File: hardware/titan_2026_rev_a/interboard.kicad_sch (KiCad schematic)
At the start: 7 parts, among them J7 B7B-XH, J8 B7B-XH, U4 ISO1642DWR

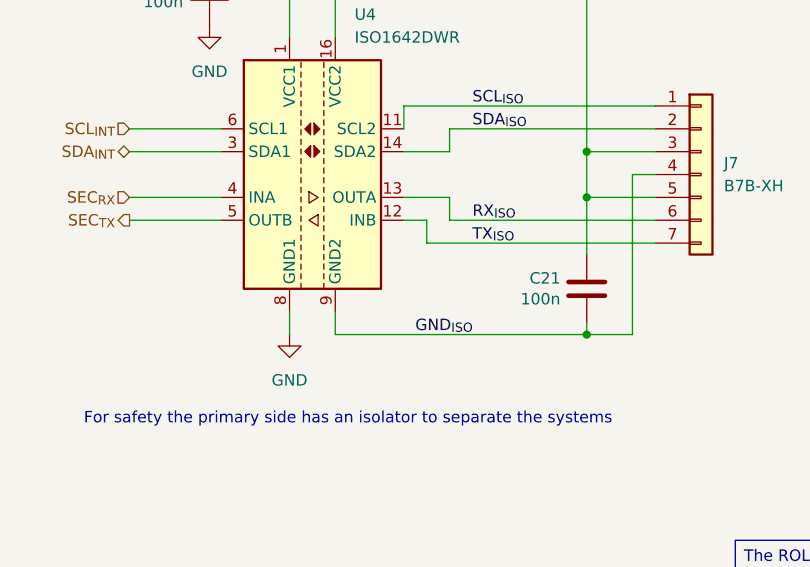
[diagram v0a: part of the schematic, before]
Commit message: Added solder bridge for connecting grounds
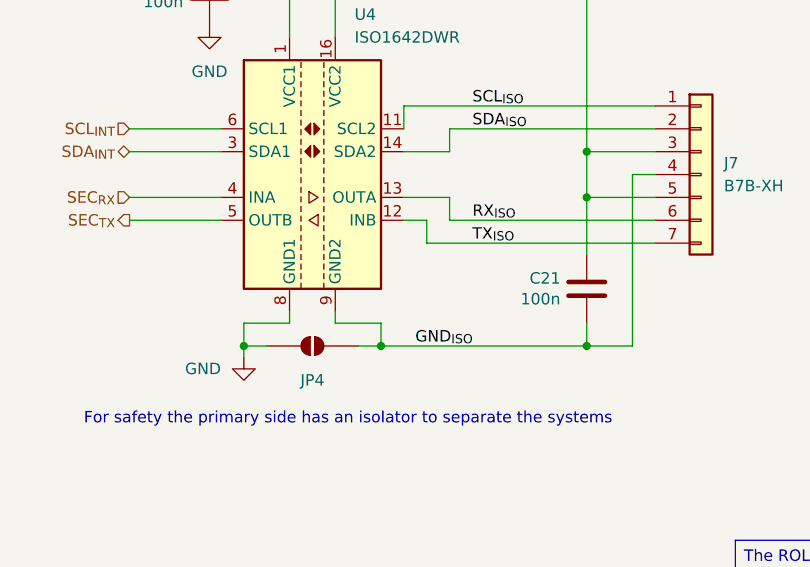
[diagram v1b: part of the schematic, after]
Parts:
- added JP4: SolderJumper_2_Open, Jumper:SolderJumper-2_P1.3mm_Open_Pad1.0x1.5mm, symbol Jumper:SolderJumper_2_Open
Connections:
- net GND: now also JP4.1 (A)
- net GND_{ISO}: now also JP4.2 (B)
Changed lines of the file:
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@@
-	)
-	(junction
-		(at 91.44 105.41)
-		(diameter 0)
-		(color 0 0 0 0)
 	)
 	(junction
@@
 	)
 	(junction
+		(at 91.44 106.68)
+		(diameter 0)
+		(color 0 0 0 0)
+	)
+	(junction
+		(at 53.34 106.68)
+		(diameter 0)
+		(color 0 0 0 0)
+	)
+	(junction
+		(at 68.58 106.68)
+		(diameter 0)
+		(color 0 0 0 0)
+	)
+	(junction
 		(at 218.44 82.55)
 		(diameter 0)
@@
 	(wire
 		(pts
-			(xy 58.42 102.87) (xy 58.42 105.41)
-		)
-		(stroke
-			(width 0)
-			(type default)
-		)
-	)
-	(wire
-		(pts
 			(xy 63.5 67.31) (xy 63.5 72.39)
 		)
@@
 	(wire
 		(pts
+			(xy 53.34 106.68) (xy 53.34 107.95)
+		)
+		(stroke
+			(width 0)
+			(type default)
+		)
+	)
+	(wire
+		(pts
 			(xy 91.44 67.31) (xy 91.44 85.09)
 		)
@@
 	(wire
 		(pts
+			(xy 66.04 106.68) (xy 68.58 106.68)
+		)
+		(stroke
+			(width 0)
+			(type default)
+		)
+	)
+	(wire
+		(pts
 			(xy 91.44 90.17) (xy 91.44 96.52)
 		)
@@
 	(wire
 		(pts
-			(xy 91.44 104.14) (xy 91.44 105.41)
-		)
-		(stroke
-			(width 0)
-			(type default)
-		)
-	)
-	(wire
-		(pts
 			(xy 205.74 92.71) (xy 229.87 92.71)
 		)
@@
 	(wire
 		(pts
+			(xy 53.34 104.14) (xy 53.34 106.68)
+		)
+		(stroke
+			(width 0)
+			(type default)
+		)
+	)
+	(wire
+		(pts
 			(xy 71.12 92.71) (xy 73.66 92.71)
 		)
@@
 	(wire
 		(pts
+			(xy 68.58 104.14) (xy 68.58 106.68)
+		)
+		(stroke
+			(width 0)
+			(type default)
+		)
+	)
+	(wire
+		(pts
 			(xy 219.71 69.85) (xy 220.98 69.85)
 		)
@@
 	(wire
 		(pts
-			(xy 96.52 87.63) (xy 96.52 105.41)
+			(xy 96.52 87.63) (xy 96.52 106.68)
 		)
 		(stroke
@@
 	(wire
 		(pts
+			(xy 53.34 104.14) (xy 58.42 104.14)
+		)
+		(stroke
+			(width 0)
+			(type default)
+		)
+	)
+	(wire
+		(pts
+			(xy 91.44 104.14) (xy 91.44 106.68)
+		)
+		(stroke
+			(width 0)
+			(type default)
+		)
+	)
+	(wire
+		(pts
+			(xy 68.58 106.68) (xy 91.44 106.68)
+		)
+		(stroke
+			(width 0)
+			(type default)
+		)
+	)
+	(wire
+		(pts
 			(xy 218.44 77.47) (xy 218.44 82.55)
 		)
@@
 	(wire
 		(pts
-			(xy 91.44 105.41) (xy 96.52 105.41)
+			(xy 91.44 106.68) (xy 96.52 106.68)
 		)
 		(stroke
@@
 	(wire
 		(pts
+			(xy 55.88 106.68) (xy 53.34 106.68)
+		)
+		(stroke
+			(width 0)
+			(type default)
+		)
+	)
+	(wire
+		(pts
 			(xy 76.2 82.55) (xy 99.06 82.55)
 		)
@@
 	(wire
 		(pts
+			(xy 58.42 104.14) (xy 58.42 102.87)
+		)
+		(stroke
+			(width 0)
+			(type default)
+		)
+	)
+	(wire
+		(pts
 			(xy 76.2 92.71) (xy 99.06 92.71)
 		)
@@
 	(wire
 		(pts
-			(xy 63.5 105.41) (xy 63.5 102.87)
-		)
-		(stroke
-			(width 0)
-			(type default)
-		)
-	)
-	(wire
-		(pts
-			(xy 63.5 105.41) (xy 91.44 105.41)
+			(xy 63.5 104.14) (xy 63.5 102.87)
+		)
+		(stroke
+			(width 0)
+			(type default)
+		)
+	)
+	(wire
+		(pts
+			(xy 63.5 104.14) (xy 68.58 104.14)
 		)
 		(stroke
@@
 	)
 	(label "GND_{ISO}"
-		(at 72.39 105.41 0)
+		(at 72.39 106.68 0)
 		(effects
 			(font
@@
 	(symbol
 		(lib_id "power:GND")
-		(at 58.42 105.41 0)
+		(at 53.34 107.95 0)
 		(unit 1)
 		(body_style 1)
@@
 		(in_pos_files yes)
 		(dnp no)
+		(fields_autoplaced yes)
 		(property "Reference" "#PWR033"
-			(at 58.42 111.76 0)
+			(at 53.34 114.3 0)
 			(hide yes)
 			(show_name no)
@@
 		)
 		(property "Value" "GND"
-			(at 58.42 110.49 0)
-			(show_name no)
-			(do_not_autoplace no)
-			(effects
-				(font
-					(size 1.27 1.27)
-				)
+			(at 50.8 109.2199 0)
+			(show_name no)
+			(do_not_autoplace no)
+			(effects
+				(font
+					(size 1.27 1.27)
+				)
+				(justify right)
 			)
 		)
 		(property "Footprint" ""
-			(at 58.42 105.41 0)
+			(at 53.34 107.95 0)
 			(hide yes)
 			(show_name no)
@@
 		)
 		(property "Datasheet" ""
-			(at 58.42 105.41 0)
+			(at 53.34 107.95 0)
 			(hide yes)
 			(show_name no)
@@
 		)
 		(property "Description" "Power symbol creates a global label with name \"GND\" , ground"
-			(at 58.42 105.41 0)
+			(at 53.34 107.95 0)
 			(hide yes)
 			(show_name no)
@@
 					(unit 1)
 				)
+			)
+		)
+	)
+	(symbol
+		(lib_id "Jumper:SolderJumper_2_Open")
+		(at 60.96 106.68 0)
+		(mirror x)
+		(unit 1)
+		(body_style 1)
+		(exclude_from_sim no)
+		(in_bom no)
+		(on_board yes)
+		(in_pos_files yes)
+		(dnp no)
+		(property "Reference" "JP4"
+			(at 60.96 110.49 0)
+			(show_name no)
+			(do_not_autoplace no)
+			(effects
+				(font
+					(size 1.27 1.27)
+				)
+			)
+		)
+		(property "Value" "SolderJumper_2_Open"
+			(at 60.96 110.49 0)
+			(hide yes)
+			(show_name no)
+			(do_not_autoplace no)
+			(effects
+				(font
+					(size 1.27 1.27)
+				)
+			)
+		)
+		(property "Footprint" "Jumper:SolderJumper-2_P1.3mm_Open_Pad1.0x1.5mm"
+			(at 60.96 106.68 0)
+			(hide yes)
+			(show_name no)
+			(do_not_autoplace no)
+			(effects
+				(font
+					(size 1.27 1.27)
+				)
+			)
+		)
+		(property "Datasheet" ""
+			(at 60.96 99.06 0)
+			(hide yes)
+			(show_name no)
+			(do_not_autoplace no)
+			(effects
+				(font
+					(size 1.27 1.27)
+				)
+			)
+		)
+		(property "Description" "Solder Jumper, 2-pole, open"
+			(at 60.96 101.6 0)
+			(hide yes)
+			(show_name no)
+			(do_not_autoplace no)
+			(effects
+				(font
+					(size 1.27 1.27)
+				)
+			)
+		)
+		(pin "1"
+		)
+		(pin "2"
+		)
+		(instances
+			(project "titan_2026_rev_a"
+				(path "/a202737f-3bef-4789-86fe-0d52089f6e3f/7ab00678-4cc7-46e5-aa8d-7c6ef8f1b87c"
+					(reference "JP4")
+					(unit 1)
+				)

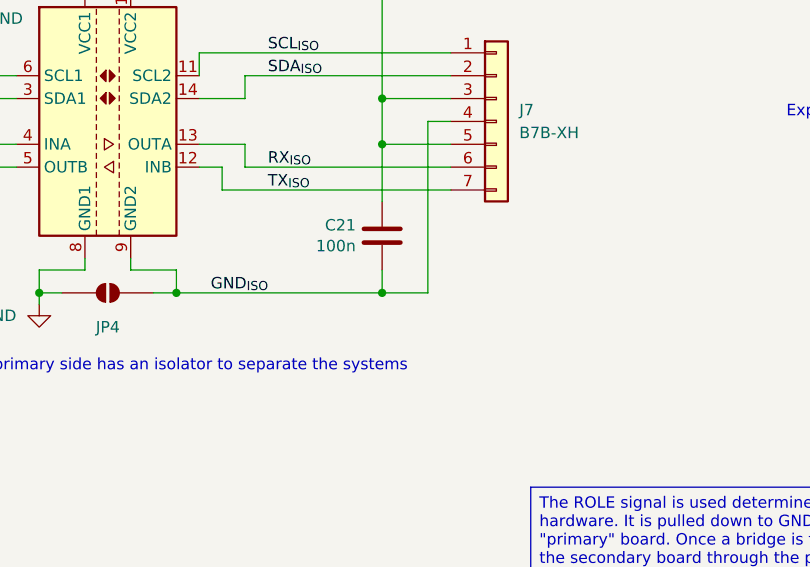
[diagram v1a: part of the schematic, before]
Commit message: Added power flag to isolated GND
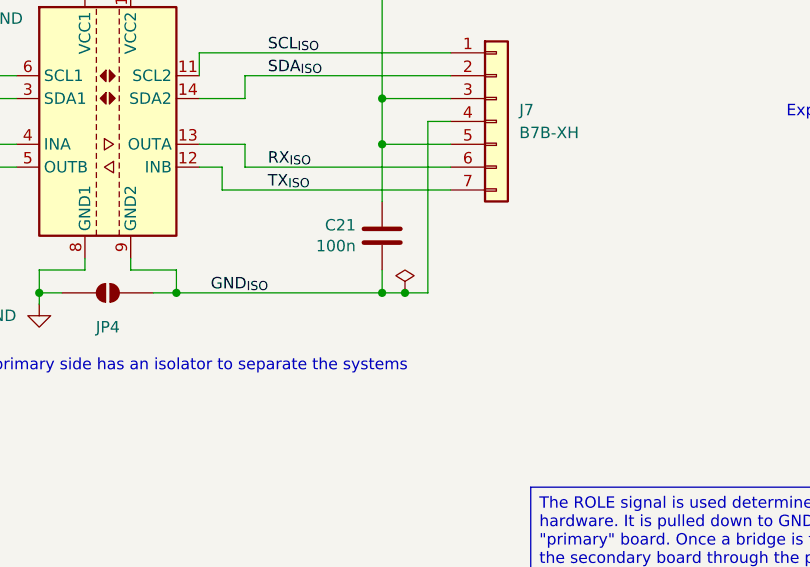
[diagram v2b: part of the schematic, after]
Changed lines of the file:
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@@
+	)
+	(junction
+		(at 93.98 106.68)
+		(diameter 0)
+		(color 0 0 0 0)
 	)
 	(junction
@@
 	(wire
 		(pts
-			(xy 91.44 106.68) (xy 96.52 106.68)
+			(xy 91.44 106.68) (xy 93.98 106.68)
 		)
 		(stroke
@@
 		(pts
 			(xy 99.06 87.63) (xy 96.52 87.63)
+		)
+		(stroke
+			(width 0)
+			(type default)
+		)
+	)
+	(wire
+		(pts
+			(xy 93.98 106.68) (xy 96.52 106.68)
 		)
 		(stroke
@@
 					(unit 1)
 				)
+			)
+		)
+	)
+	(symbol
+		(lib_id "power:PWR_FLAG")
+		(at 93.98 106.68 0)
+		(unit 1)
+		(body_style 1)
+		(exclude_from_sim no)
+		(in_bom yes)
+		(on_board yes)
+		(in_pos_files yes)
+		(dnp no)
+		(fields_autoplaced yes)
+		(property "Reference" "#FLG08"
+			(at 93.98 104.775 0)
+			(hide yes)
+			(show_name no)
+			(do_not_autoplace no)
+			(effects
+				(font
+					(size 1.27 1.27)
+				)
+			)
+		)
+		(property "Value" "PWR_FLAG"
+			(at 93.98 102.87 0)
+			(hide yes)
+			(show_name no)
+			(do_not_autoplace no)
+			(effects
+				(font
+					(size 1.27 1.27)
+				)
+			)
+		)
+		(property "Footprint" ""
+			(at 93.98 106.68 0)
+			(hide yes)
+			(show_name no)
+			(do_not_autoplace no)
+			(effects
+				(font
+					(size 1.27 1.27)
+				)
+			)
+		)
+		(property "Datasheet" ""
+			(at 93.98 106.68 0)
+			(hide yes)
+			(show_name no)
+			(do_not_autoplace no)
+			(effects
+				(font
+					(size 1.27 1.27)
+				)
+			)
+		)
+		(property "Description" "Special symbol for telling ERC where power comes from"
+			(at 93.98 106.68 0)
+			(hide yes)
+			(show_name no)
+			(do_not_autoplace no)
+			(effects
+				(font
+					(size 1.27 1.27)
+				)
+			)
+		)
+		(pin "1"
+		)
+		(instances
+			(project "titan_2026_rev_a"
+				(path "/a202737f-3bef-4789-86fe-0d52089f6e3f/7ab00678-4cc7-46e5-aa8d-7c6ef8f1b87c"
+					(reference "#FLG08")
+					(unit 1)
+				)
